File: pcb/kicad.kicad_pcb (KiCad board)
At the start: 2 copper layers, 70 x 70 mm, 16 parts, among them SW1 SW_Push, SW2 SW_SPDT, U2 ATtiny85-20P

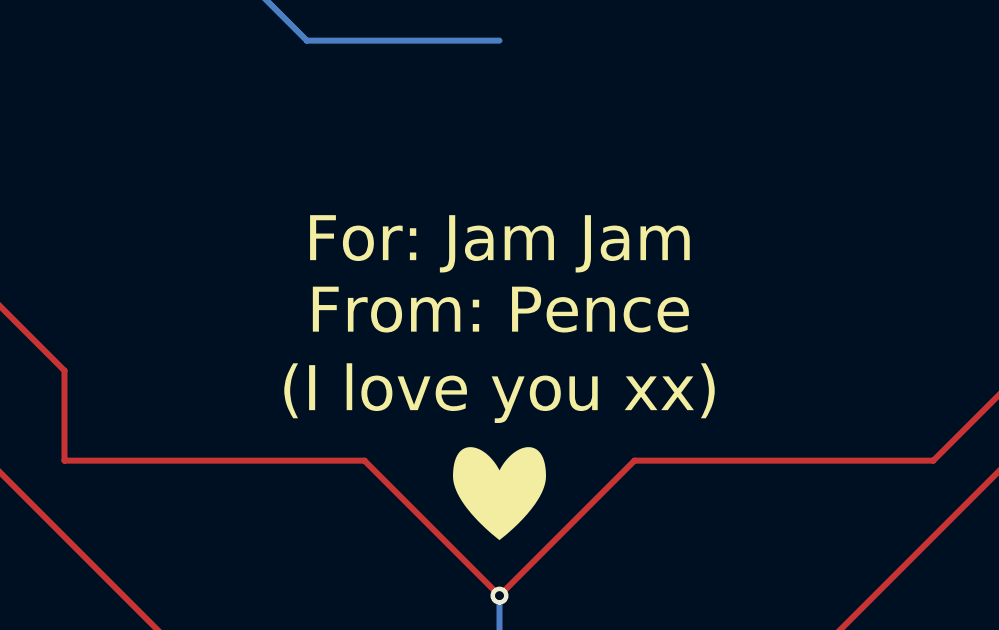
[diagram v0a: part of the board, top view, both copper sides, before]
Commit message: Making sure Project Luminescence won't get denied upon review
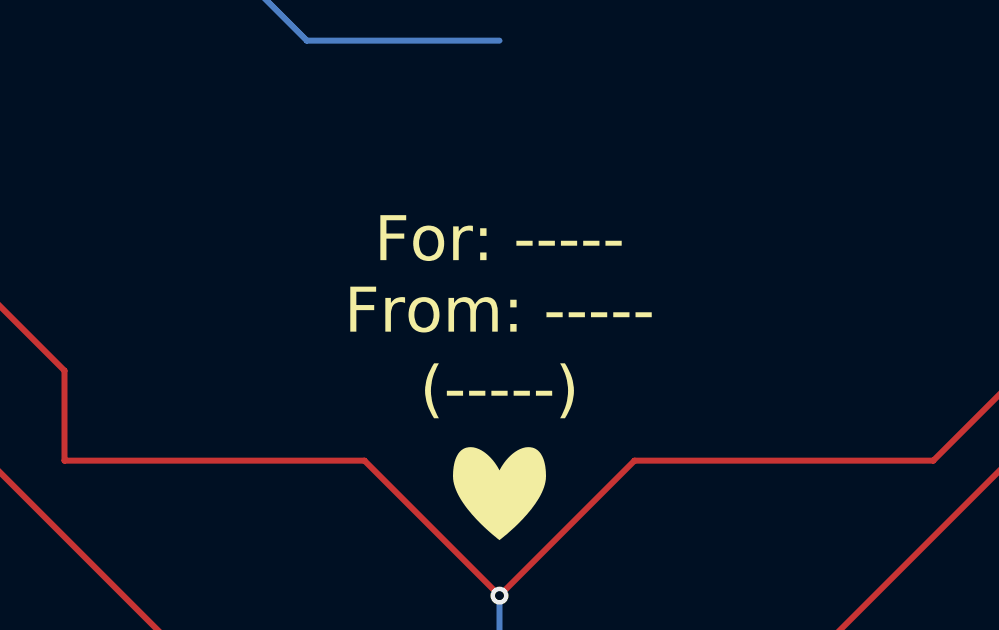
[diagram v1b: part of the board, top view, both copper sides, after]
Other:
- board text added: "(-----)"
- board text added: "For: -----"
- board text added: "From: -----"
- board text removed: "(I love you xx)"
- board text removed: "For: Jam Jam"
- board text removed: "From: Pence"
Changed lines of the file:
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@@
 (kicad_pcb
-	(version 20260616)
+	(version 20260901)
 	(generator "pcbnew")
 	(generator_version "10.99")
@@
 		(tags "LED")
 		(property "Reference" "D10"
-			(at 1.27 4 360)
+			(at 1.27 4 0)
 			(layer "F.SilkS")
 			(effects
@@
 		)
 		(property "Value" "LED"
-			(at 1.27 -4 360)
+			(at 1.27 -4 0)
 			(layer "F.Fab")
 			(effects
@@
 		)
 		(property "Datasheet" ""
-			(at 0 0 360)
+			(at 0 0 0)
 			(layer "F.Fab")
 			(hide yes)
@@
 		)
 		(property "Description" "Light emitting diode"
-			(at 0 0 360)
+			(at 0 0 0)
 			(layer "F.Fab")
 			(hide yes)
@@
 		)
 		(property "KiLib_Generator" "LED/THT"
-			(at 0 0 360)
+			(at 0 0 0)
 			(layer "F.SilkS")
 			(hide yes)
@@
 		)
 		(fp_text user "${REFERENCE}"
-			(at 1.27 0 360)
+			(at 1.27 0 0)
 			(layer "F.Fab")
 			(effects
@@
 		(tags "LED")
 		(property "Reference" "D8"
-			(at 1.27 4 360)
+			(at 1.27 4 0)
 			(layer "F.SilkS")
 			(effects
@@
 		)
 		(property "Value" "LED"
-			(at 1.27 -4 360)
+			(at 1.27 -4 0)
 			(layer "F.Fab")
 			(effects
@@
 		)
 		(property "Datasheet" ""
-			(at 0 0 360)
+			(at 0 0 0)
 			(layer "F.Fab")
 			(hide yes)
@@
 		)
 		(property "Description" "Light emitting diode"
-			(at 0 0 360)
+			(at 0 0 0)
 			(layer "F.Fab")
 			(hide yes)
@@
 		)
 		(property "KiLib_Generator" "LED/THT"
-			(at 0 0 360)
+			(at 0 0 0)
 			(layer "F.SilkS")
 			(hide yes)
@@
 		)
 		(fp_text user "${REFERENCE}"
-			(at 1.27 0 360)
+			(at 1.27 0 0)
 			(layer "F.Fab")
 			(effects
@@
 		)
 		(property "Sim.Pins" "1=K 2=A"
-			(at 0 0 -90)
+			(at 0 0 270)
 			(unlocked yes)
 			(layer "F.Fab")
@@
 		)
 		(pad "1" thru_hole rect
-			(at 0 0 -90)
+			(at 0 0 270)
 			(size 1.8 1.8)
 			(drill 0.9)
@@
 		)
 		(pad "2" thru_hole circle
-			(at 2.54 0 -90)
+			(at 2.54 0 270)
 			(size 1.8 1.8)
 			(drill 0.9)
@@
 		(tags "LED")
 		(property "Reference" "D9"
-			(at 1.27 4 360)
+			(at 1.27 4 0)
 			(layer "F.SilkS")
 			(effects
@@
 		)
 		(property "Value" "LED"
-			(at 1.27 -4 360)
+			(at 1.27 -4 0)
 			(layer "F.Fab")
 			(effects
@@
 		)
 		(property "Datasheet" ""
-			(at 0 0 360)
+			(at 0 0 0)
 			(layer "F.Fab")
 			(hide yes)
@@
 		)
 		(property "Description" "Light emitting diode"
-			(at 0 0 360)
+			(at 0 0 0)
 			(layer "F.Fab")
 			(hide yes)
@@
 		)
 		(property "KiLib_Generator" "LED/THT"
-			(at 0 0 360)
+			(at 0 0 0)
 			(layer "F.SilkS")
 			(hide yes)
@@
 		)
 		(fp_text user "${REFERENCE}"
-			(at 1.27 0 360)
+			(at 1.27 0 0)
 			(layer "F.Fab")
 			(effects
@@
 		)
 		(property "Description" "Single-cell battery"
-			(at 12.4 0 -90)
+			(at 12.4 0 270)
 			(unlocked yes)
 			(layer "B.Fab")
@@
 		(tags "Potentiometer Trimmer RM-065")
 		(property "Reference" "RV1"
-			(at 2.6 2.5 360)
+			(at 2.6 2.5 0)
 			(layer "B.SilkS")
 			(effects
@@
 		)
 		(property "Value" "Trimpot"
-			(at 2.6 -7.4 360)
+			(at 2.6 -7.4 0)
 			(layer "B.Fab")
 			(effects
@@
 		)
 		(property "Datasheet" ""
-			(at 0 0 360)
+			(at 0 0 0)
 			(unlocked yes)
 			(layer "B.Fab")
@@
 		)
 		(property "Description" "Trim-potentiometer"
-			(at 0 0 360)
+			(at 0 0 0)
 			(unlocked yes)
 			(layer "B.Fab")
@@
 		)
 		(fp_text user "${REFERENCE}"
-			(at 2.5 -2.5 360)
+			(at 2.5 -2.5 0)
 			(layer "B.Fab")
 			(effects
@@
 		(tags "THT DIP DIL PDIP 2.54mm 7.62mm 300mil")
 		(property "Reference" "U2"
-			(at 3.81 2.33 360)
+			(at 3.81 2.33 0)
 			(layer "B.SilkS")
 			(effects
@@
 		)
 		(property "Value" "ATtiny85-20P"
-			(at 3.81 -9.95 360)
+			(at 3.81 -9.95 0)
 			(layer "B.Fab")
 			(effects
@@
 		)
 		(property "Datasheet" "http://ww1.microchip.com/downloads/en/DeviceDoc/atmel-2586-avr-8-bit-microcontroller-attiny25-attiny45-attiny85_datasheet.pdf"
-			(at 0 0 360)
+			(at 0 0 0)
 			(layer "B.Fab")
 			(hide yes)
@@
 		)
 		(property "Description" "20MHz, 8kB Flash, 512B SRAM, 512B EEPROM, debugWIRE, DIP-8"
-			(at 0 0 360)
+			(at 0 0 0)
 			(layer "B.Fab")
 			(hide yes)
@@
 		)
 		(property "KiLib_Generator" "package/DIP/legacy"
-			(at 0 0 360)
+			(at 0 0 0)
 			(layer "B.SilkS")
 			(hide yes)
@@
 		)
 		(fp_text user "${REFERENCE}"
-			(at 3.81 -3.81 450)
+			(at 3.81 -3.81 90)
 			(layer "B.Fab")
 			(effects
@@
 		(tags "switch single-pole opposite-side-connection double-throw SPDT würth wurth")
 		(property "Reference" "SW2"
-			(at 0 2.54 360)
+			(at 0 2.54 0)
 			(layer "B.SilkS")
 			(effects
@@
 		)
 		(property "Value" "SW_SPDT"
-			(at 0 -3.81 360)
+			(at 0 -3.81 0)
 			(layer "B.Fab")
 			(effects
@@
 		)
 		(property "Datasheet" ""
-			(at 0 0 360)
+			(at 0 0 0)
 			(unlocked yes)
 			(layer "B.Fab")
@@
 		)
 		(property "Description" "Switch, single pole double throw"
-			(at 0 0 360)
+			(at 0 0 0)
 			(unlocked yes)
 			(layer "B.Fab")
@@
 		)
 		(fp_text user "${REFERENCE}"
-			(at 0 -2.54 360)
+			(at 0 -2.54 0)
 			(layer "B.Fab")
 			(effects
@@
 		(layer "Edge.Cuts")
 	)
-	(gr_text "For: Jam Jam"
+	(gr_text "For: -----"
 		(at 141 107 0)
 		(layer "F.SilkS")
@@
 		)
 	)
-	(gr_text "From: Pence"
+	(gr_text "From: -----"
 		(at 141 109.38347 0)
 		(layer "F.SilkS")
@@
 		)
 	)
-	(gr_text "(I love you xx)"
+	(gr_text "(-----)"
 		(at 141 112 0)
 		(layer "F.SilkS")
